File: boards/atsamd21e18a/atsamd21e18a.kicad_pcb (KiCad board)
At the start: 4 copper layers, 17.8 x 38.1 mm, 25 parts, among them J1 USB_B_Micro, J2 A, J3 B, J4 SWD_1.27, SW1 RESET, U1 AP7361C_SOT-89-5, U2 ATSAMD21E, Y1 ABS07-32.768KHZ

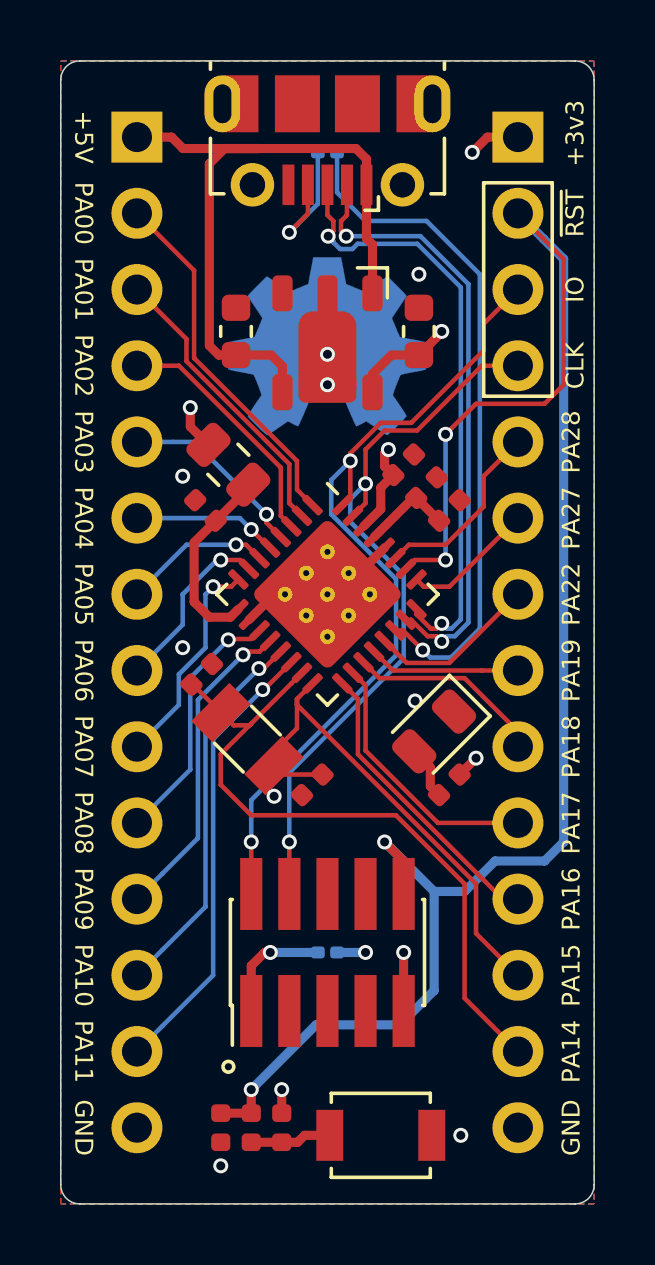
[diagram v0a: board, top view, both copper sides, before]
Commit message: Fixed errors in main README. Added boards.
Accidentally committed changes to ice40hx8k-bg121 and atsamd21e18a
boards.

The ice40hx8k-bg121 changes include adding access to CBSEL0/1 and
rerouting IO.

The atsamd21e18a changes include rerouting IO to prioritize USB
D+/- routing.
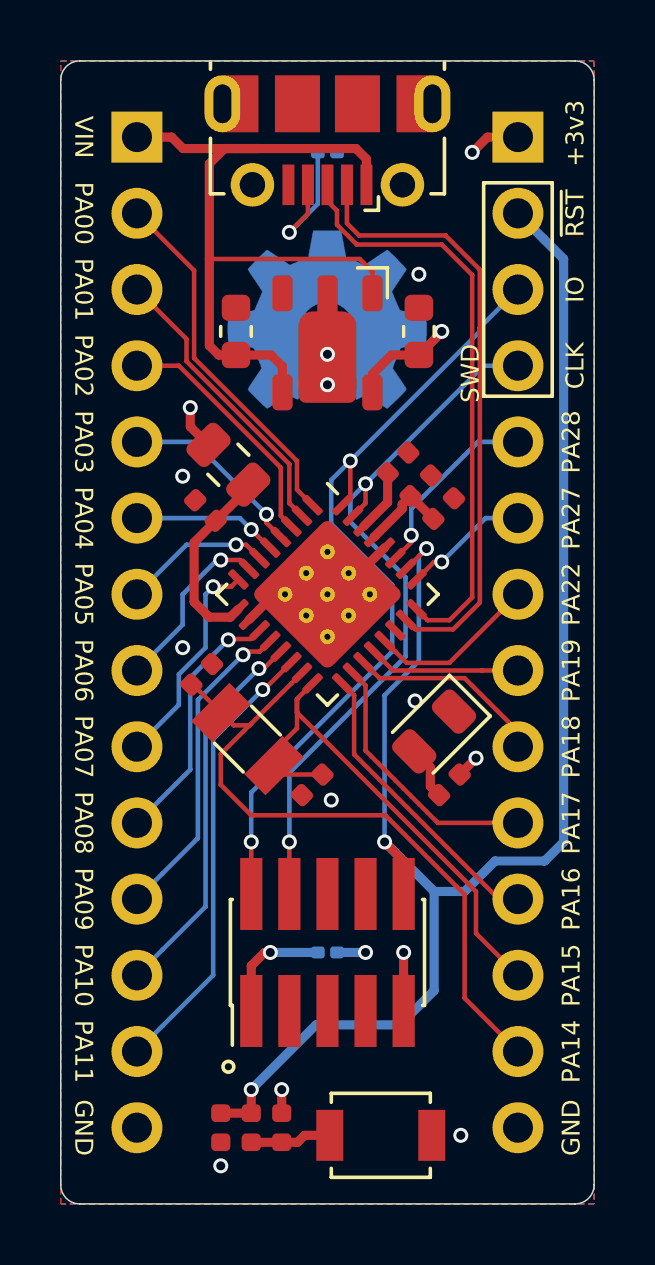
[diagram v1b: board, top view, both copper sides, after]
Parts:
- moved REF** 0.89 mm to (35.6, 31.5)
- moved C3 0.20 mm to (38.7, 37.0)
- moved C5 0.20 mm to (37.9, 36.3)
- moved C2 0.20 mm to (39.4, 37.8)
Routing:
- net /PA23: track 22.6 -> 0.00 mm, vias 1 -> 0
- net /~RESET: track 60.1 -> 54.8 mm, vias 4 -> 3
- net +5V: track 24.0 -> 26.7 mm
- net +3V3: track 12.4 -> 11.4 mm, vias 7 -> 6
- net /SWD_IO: track 27.8 -> 27.1 mm
- net /SWD_CLK: track 24.8 -> 24.2 mm
- net /USB_D+: track 20.3 -> 19.7 mm, vias 2 -> 0
- net /PA27: track 4.43 -> 4.23 mm, vias 0 -> 1
- net /USB_D-: track 20.5 -> 20.4 mm, vias 2 -> 0
- net /PA28: track 6.29 -> 6.35 mm, vias 0 -> 1
- net GND: vias 9 -> 10
- net /PA15: vias 1 -> 0
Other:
- board text added: "SWD"
- board text added: "VIN"
- board text added: "atsamd21e18a 2020-02 fourside.io"
- board text removed: "+5V"
- board text removed: "atsamd21e18a breakout fourside.io"

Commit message: Techincally, reworked routing. Finished 3v3 and SOF 1 kHz routing.
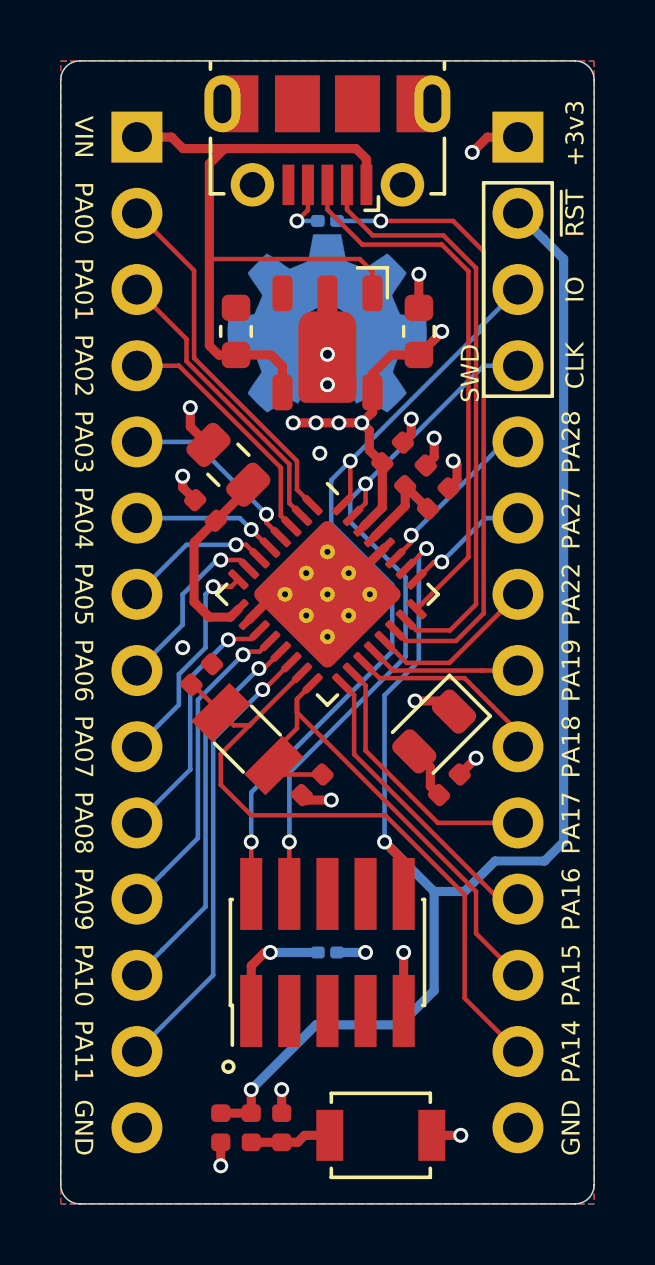
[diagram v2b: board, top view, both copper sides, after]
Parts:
- moved JP1 2.29 mm to (35.6, 28.2)
- moved C2 0.38 mm to (39.3, 37.5)
- moved C3 0.38 mm to (38.5, 36.7)
- moved C5 0.38 mm to (37.7, 35.9)
- moved REF** 0.13 mm to (35.6, 31.6)
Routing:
- net /PA23: track 0.00 -> 20.8 mm, vias 0 -> 1
- net GND: track 7.47 -> 16.8 mm, vias 10 -> 14
- net +3V3: track 11.4 -> 16.7 mm, vias 6 -> 10
- net /USB_SOF: track 4.90 -> 2.05 mm
- net /USB_D+: track 19.7 -> 18.4 mm
- net /PA28: track 6.35 -> 5.83 mm
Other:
- board text removed: "SOF PA23"
- board text removed: "SWD 3v3"

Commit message: Removed solder jumpers for USB SOF/ID and SWD 3v3.
Fixes issue #6. Fixes issue #8.
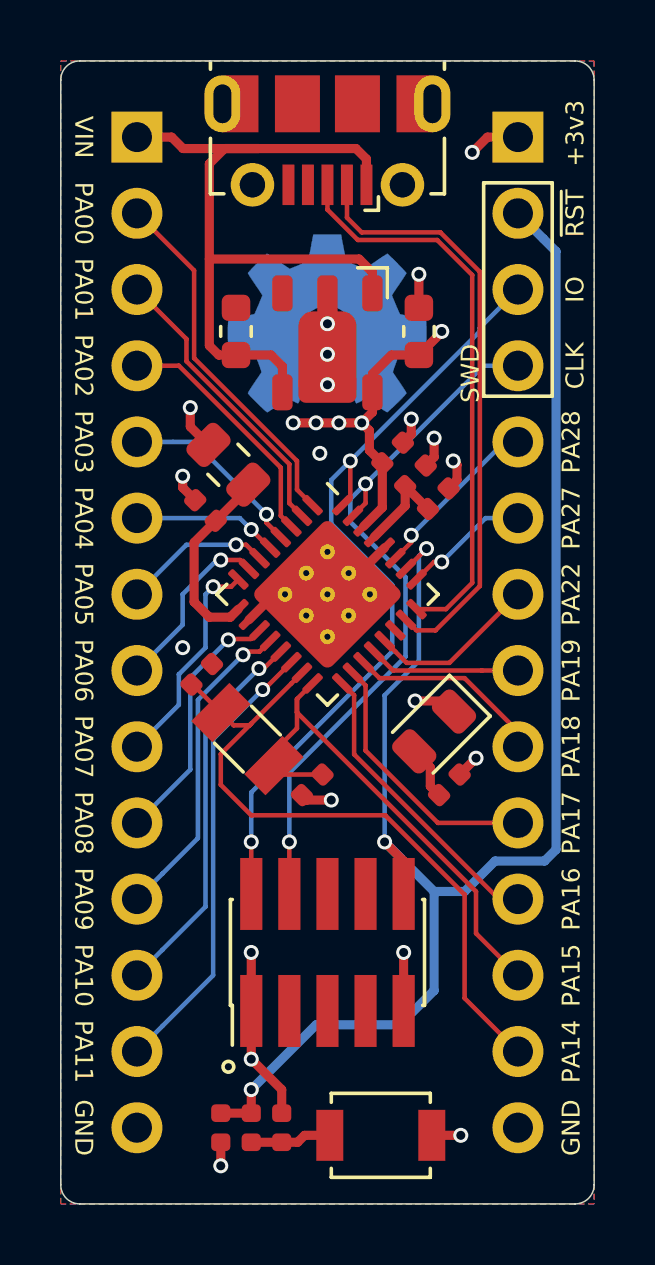
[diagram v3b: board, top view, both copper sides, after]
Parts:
- removed JP1: USB_SOF, Resistor_SMD:R_0201_0603Metric
- removed JP2: SWD_VCC, Resistor_SMD:R_0201_0603Metric
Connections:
- J1 pad 4: /USB_SOF -> Net-(J1-Pad4)
- J4 pad 1: /SWD_3V3 -> +3V3
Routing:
- net /PA23: track 20.8 -> 0.00 mm, vias 1 -> 0
- net +3V3: track 16.7 -> 20.7 mm
- net /SWD_3V3: track 3.91 -> 0.00 mm, vias 1 -> 0
- net /USB_SOF: track 2.05 -> 0.00 mm, vias 1 -> 0
- net /USB_D+: track 18.4 -> 19.0 mm
- net GND: vias 14 -> 15
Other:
- board text added: "atsamd21e18a 2020-03 fourside.io"
- board text removed: "atsamd21e18a 2020-02 fourside.io"

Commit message: Added filter to USB. Added USB shield zone to F.Cu and B.Cu.
Fixes issue #7.
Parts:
- added C10: 0.01u, Capacitor_SMD:C_0402_1005Metric, F.Cu at (34.7, 28.7)
- added R4: 100k, Resistor_SMD:R_0402_1005Metric, F.Cu at (32.8, 28.7)
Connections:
- J1 pad 6: GND -> /USB_SHIELD
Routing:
- net GND: track 16.8 -> 22.1 mm, vias 15 -> 17
- net /USB_SHIELD: track 0.00 -> 2.73 mm
- added copper zone on B.Cu, net /USB_SHIELD
- added copper zone on F.Cu, net /USB_SHIELD

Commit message: Version 2020-04 looks good. Next: panelize.
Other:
- board text added: "atsamd21e18a 2020-04 fourside.io"
- board text removed: "atsamd21e18a 2020-03 fourside.io"
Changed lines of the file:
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@@
   (general
     (thickness 1.6)
-    (drawings 43)
+    (drawings 57)
     (tracks 314)
     (zones 0)
@@
   )
   (setup
-    (last_trace_width 0.3048)
+    (last_trace_width 0.1524)
     (user_trace_width 0.1524)
     (user_trace_width 0.2032)
@@
     )
   )
+  (gr_text PA06 (at 27.432 43.18 270) (layer F.SilkS)
+    (effects (font (size 0.6 0.6) (thickness 0.1)))
+  )
+  (gr_text PA11 (at 27.432 55.88 270) (layer F.SilkS)
+    (effects (font (size 0.6 0.6) (thickness 0.1)))
+  )
+  (gr_text PA01 (at 27.432 30.48 270) (layer F.SilkS)
+    (effects (font (size 0.6 0.6) (thickness 0.1)))
+  )
+  (gr_text PA02 (at 27.432 33.02 270) (layer F.SilkS)
+    (effects (font (size 0.6 0.6) (thickness 0.1)))
+  )
+  (gr_text PA00 (at 27.432 27.94 270) (layer F.SilkS)
+    (effects (font (size 0.6 0.6) (thickness 0.1)))
+  )
+  (gr_text PA10 (at 27.432 53.34 270) (layer F.SilkS)
+    (effects (font (size 0.6 0.6) (thickness 0.1)))
+  )
+  (gr_text PA04 (at 27.432 38.1 270) (layer F.SilkS)
+    (effects (font (size 0.6 0.6) (thickness 0.1)))
+  )
+  (gr_text PA05 (at 27.432 40.64 270) (layer F.SilkS)
+    (effects (font (size 0.6 0.6) (thickness 0.1)))
+  )
+  (gr_text VIN (at 27.432 25.4 270) (layer F.SilkS)
+    (effects (font (size 0.6 0.6) (thickness 0.1)))
+  )
+  (gr_text PA07 (at 27.432 45.72 270) (layer F.SilkS)
+    (effects (font (size 0.6 0.6) (thickness 0.1)))
+  )
+  (gr_text GND (at 27.432 58.42 270) (layer F.SilkS)
+    (effects (font (size 0.6 0.6) (thickness 0.1)))
+  )
+  (gr_text PA03 (at 27.432 35.56 270) (layer F.SilkS)
+    (effects (font (size 0.6 0.6) (thickness 0.1)))
+  )
+  (gr_text PA08 (at 27.432 48.26 270) (layer F.SilkS)
+    (effects (font (size 0.6 0.6) (thickness 0.1)))
+  )
+  (gr_text PA09 (at 27.432 50.8 270) (layer F.SilkS)
+    (effects (font (size 0.6 0.6) (thickness 0.1)))
+  )
   (gr_text SWD (at 40.3225 33.274 90) (layer F.SilkS)
     (effects (font (size 0.6 0.6) (thickness 0.1)))
@@
     (effects (font (size 0.6 0.6) (thickness 0.1)))
   )
-  (gr_text "atsamd21e18a\n2020-03\nfourside.io" (at 40.005 58.928) (layer B.Mask)
+  (gr_text "atsamd21e18a\n2020-04\nfourside.io" (at 40.005 58.928) (layer B.Mask)
     (effects (font (size 0.6 0.6) (thickness 0.1)) (justify left mirror))
   )
@@
   (gr_line (start 43.815 60.96) (end 27.305 60.96) (layer Edge.Cuts) (width 0.05))
   (gr_line (start 27.305 22.86) (end 43.815 22.86) (layer Edge.Cuts) (width 0.05))
-  (via (at 32.1945 27.8765) (size 0.5) (drill 0.3) (layers F.Cu B.Cu) (net 2))
   (via (at 40.386 25.908) (size 0.5) (drill 0.3) (layers F.Cu B.Cu) (net 1))
   (segment (start 41.91 25.4) (end 40.894 25.4) (width 0.3048) (layer F.Cu) (net 1))
@@
   (via (at 33.02 52.577996) (size 0.5) (drill 0.3) (layers F.Cu B.Cu) (net 1))
   (segment (start 33.02 54.528) (end 33.02 52.577996) (width 0.3048) (layer F.Cu) (net 1))
+  (via (at 32.1945 27.8765) (size 0.5) (drill 0.3) (layers F.Cu B.Cu) (net 2))
   (via (at 35.56 33.655) (size 0.5) (drill 0.3) (layers F.Cu B.Cu) (net 2))
   (via (at 35.56 32.639) (size 0.5) (drill 0.3) (layers F.Cu B.Cu) (net 2))
@@
   (segment (start 32.43338 45.00638) (end 32.961388 45.00638) (width 0.1524) (layer F.Cu) (net 5))
   (segment (start 32.009117 44.582117) (end 32.43338 45.00638) (width 0.1524) (layer F.Cu) (net 5))
-  (segment (start 33.014884 44.952884) (end 34.35792 43.609847) (width 0.1524) (layer F.Cu) (net 5))
   (segment (start 31.076947 43.649947) (end 32.009117 44.582117) (width 0.1524) (layer F.Cu) (net 5))
   (segment (start 31.026053 43.649947) (end 31.076947 43.649947) (width 0.1524) (layer F.Cu) (net 5))
-  (segment (start 33.02 48.006) (end 32.004 46.99) (width 0.1524) (layer F.Cu) (net 5))
-  (segment (start 32.004 46.99) (end 32.004 45.963767) (width 0.1524) (layer F.Cu) (net 5))
-  (segment (start 37.486776 48.006) (end 33.02 48.006) (width 0.1524) (layer F.Cu) (net 5))
   (segment (start 40.132 50.651224) (end 37.486776 48.006) (width 0.1524) (layer F.Cu) (net 5))
   (segment (start 40.132 54.102) (end 40.132 50.651224) (width 0.1524) (layer F.Cu) (net 5))
   (segment (start 41.91 55.88) (end 40.132 54.102) (width 0.1524) (layer F.Cu) (net 5))
+  (segment (start 33.014884 44.952884) (end 34.35792 43.609847) (width 0.1524) (layer F.Cu) (net 5))
   (segment (start 32.004 45.963767) (end 33.014884 44.952884) (width 0.1524) (layer F.Cu) (net 5))
+  (segment (start 32.004 46.99) (end 32.004 45.963767) (width 0.1524) (layer F.Cu) (net 5))
+  (segment (start 33.02 48.006) (end 32.004 46.99) (width 0.1524) (layer F.Cu) (net 5))
+  (segment (start 37.486776 48.006) (end 33.02 48.006) (width 0.1524) (layer F.Cu) (net 5))
   (segment (start 34.544 45.108726) (end 33.791305 45.861421) (width 0.1524) (layer F.Cu) (net 6))
   (segment (start 35.065025 43.609848) (end 34.544 44.130873) (width 0.1524) (layer F.Cu) (net 6))

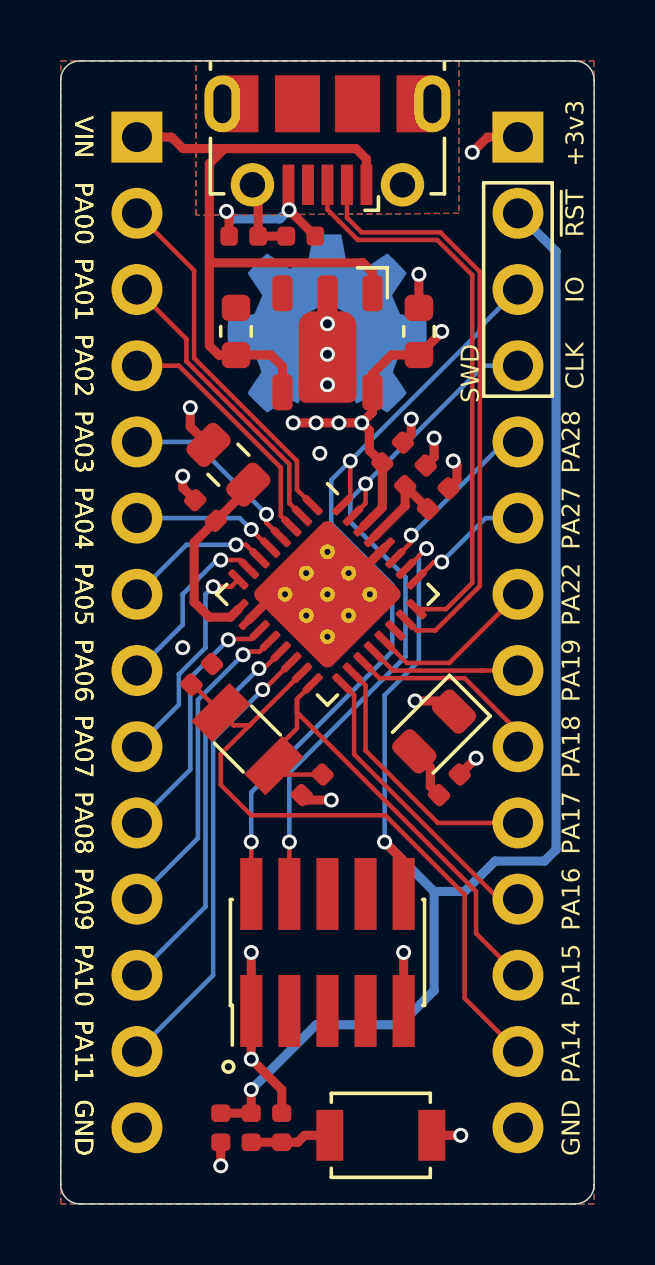
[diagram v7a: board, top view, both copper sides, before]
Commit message: N.O. Jumpers for PA14 and PA15.
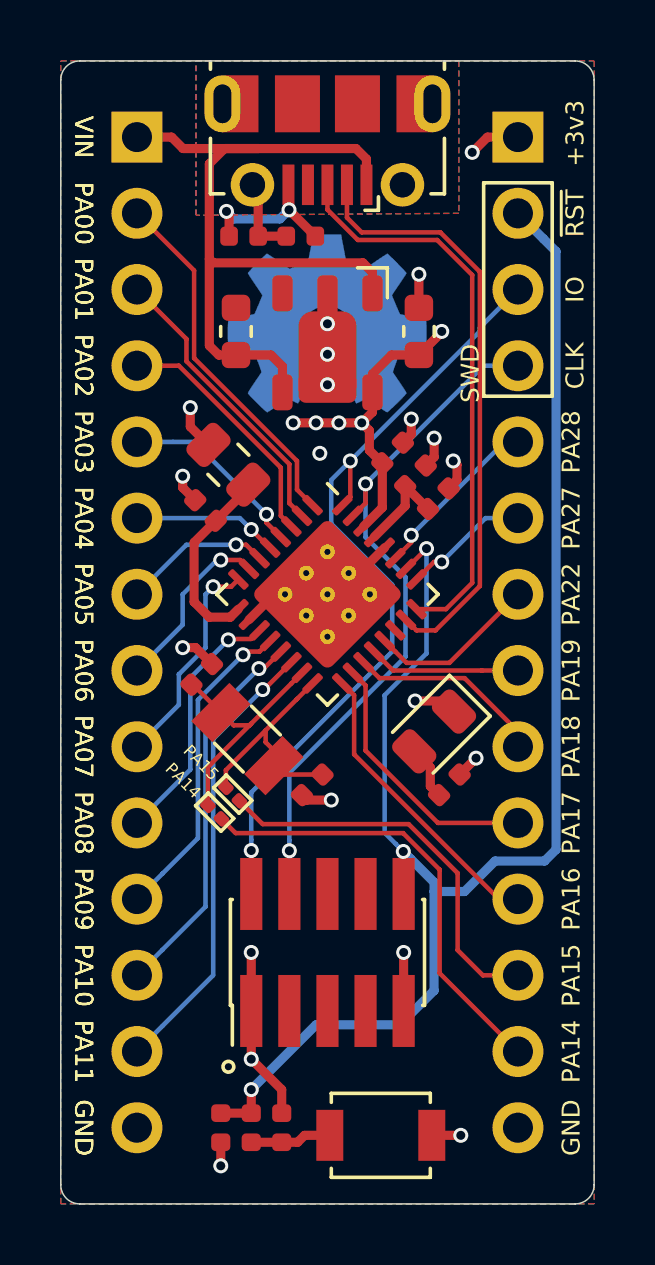
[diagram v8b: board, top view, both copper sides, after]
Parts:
- added PA14: J_PA14, jkiv-library:J_NO_0201_0603Metric, F.Cu at (31.8, 47.9)
- added PA15: J_PA15, jkiv-library:J_NO_0201_0603Metric, F.Cu at (32.4, 47.3)
- R1: value 100R -> 4k7
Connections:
- J3 pad 12: /PA15 -> /PA15_NO
- J3 pad 13: /PA14 -> /PA14_NO
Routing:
- net /PA14_NO: track 0.00 -> 15.1 mm
- net /PA14: track 23.0 -> 8.29 mm
- net /PA15_NO: track 0.00 -> 13.2 mm
- net /PA15: track 16.8 -> 7.21 mm
- net GND: track 22.1 -> 23.3 mm
- net /~RESET: track 54.6 -> 54.0 mm
